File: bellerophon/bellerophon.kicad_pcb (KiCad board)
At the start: 4 copper layers, 35 x 90 mm, 45 parts, among them Q1 ST3413A, Q2 IRLL014NPBF, Q3 IRLL014NPBF, U1 HT7350-A, U2 BNO055, U3 MPL3115A2, U4 Teensy4.0, U5 XTSD, Y1 32.768kHz

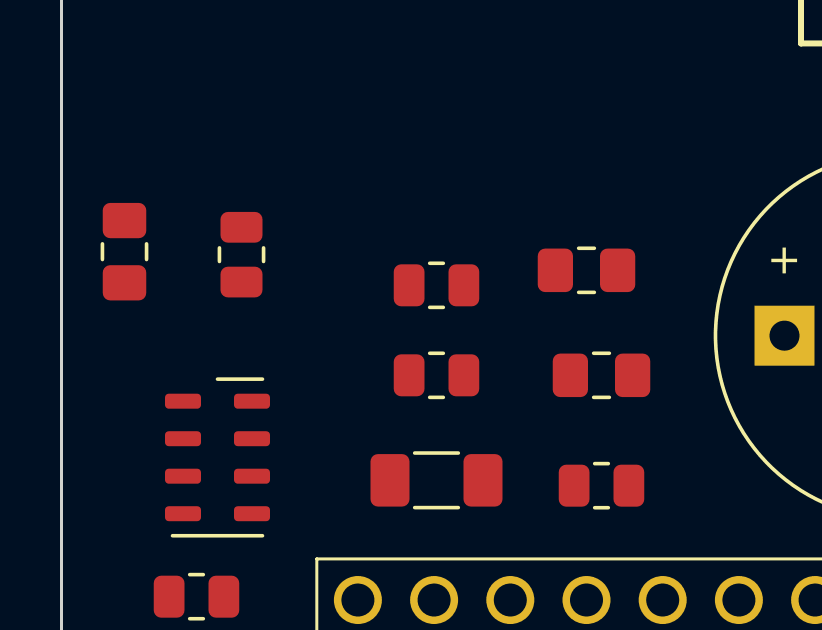
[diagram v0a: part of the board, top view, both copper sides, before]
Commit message: change pin assignments to better fit layout
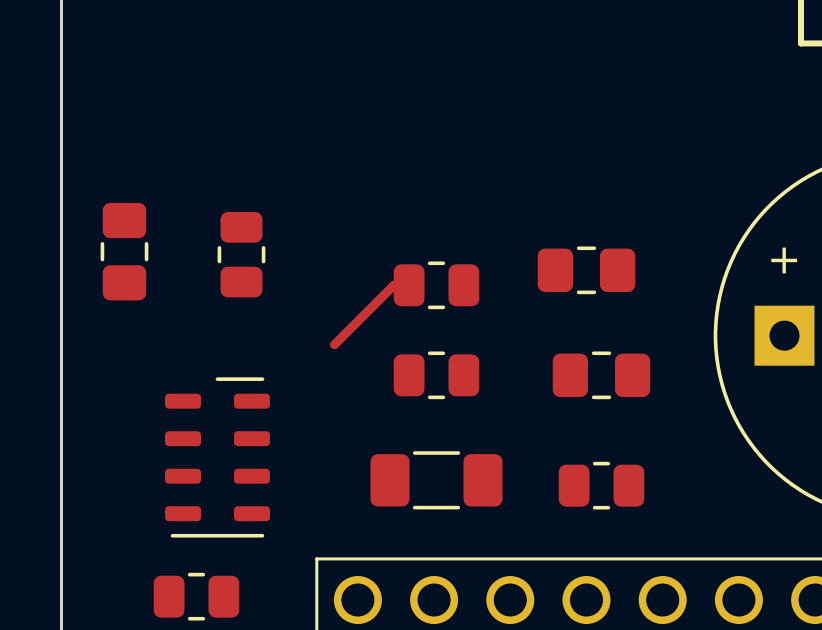
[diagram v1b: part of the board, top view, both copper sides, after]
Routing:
- net /SDA0: track 0.00 -> 3.31 mm
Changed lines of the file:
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@@
   )
   (segment (start 207.65 115.7) (end 207.65 116.3) (width 0.3) (layer "F.Cu") (net 1))
+  (segment (start 213.57868 103.62132) (end 211.6 105.6) (width 0.3) (layer "F.Cu") (net 12))
+  (segment (start 214.0875 103.62132) (end 213.57868 103.62132) (width 0.3) (layer "F.Cu") (net 12))
 )

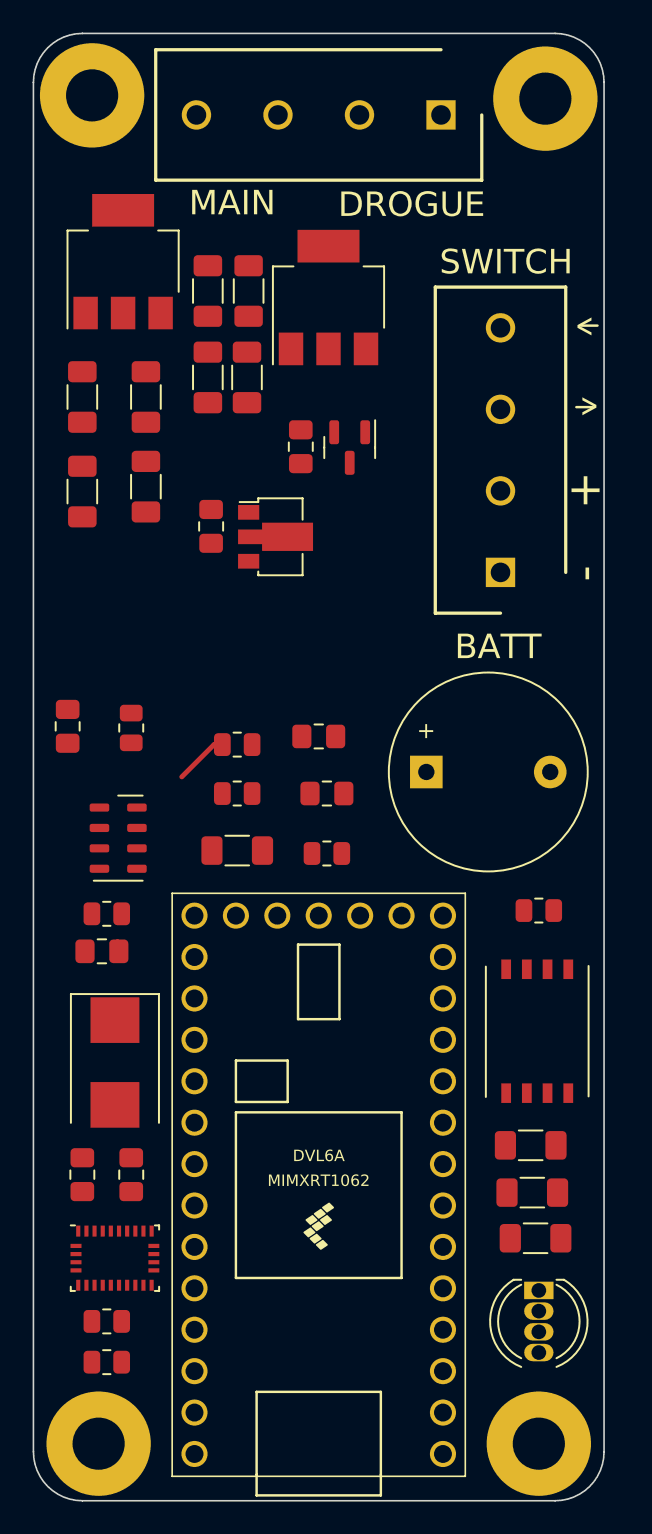
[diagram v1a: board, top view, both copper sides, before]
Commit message: change pyro mosfet to smaller SOT-23, shrink board to 85 mm
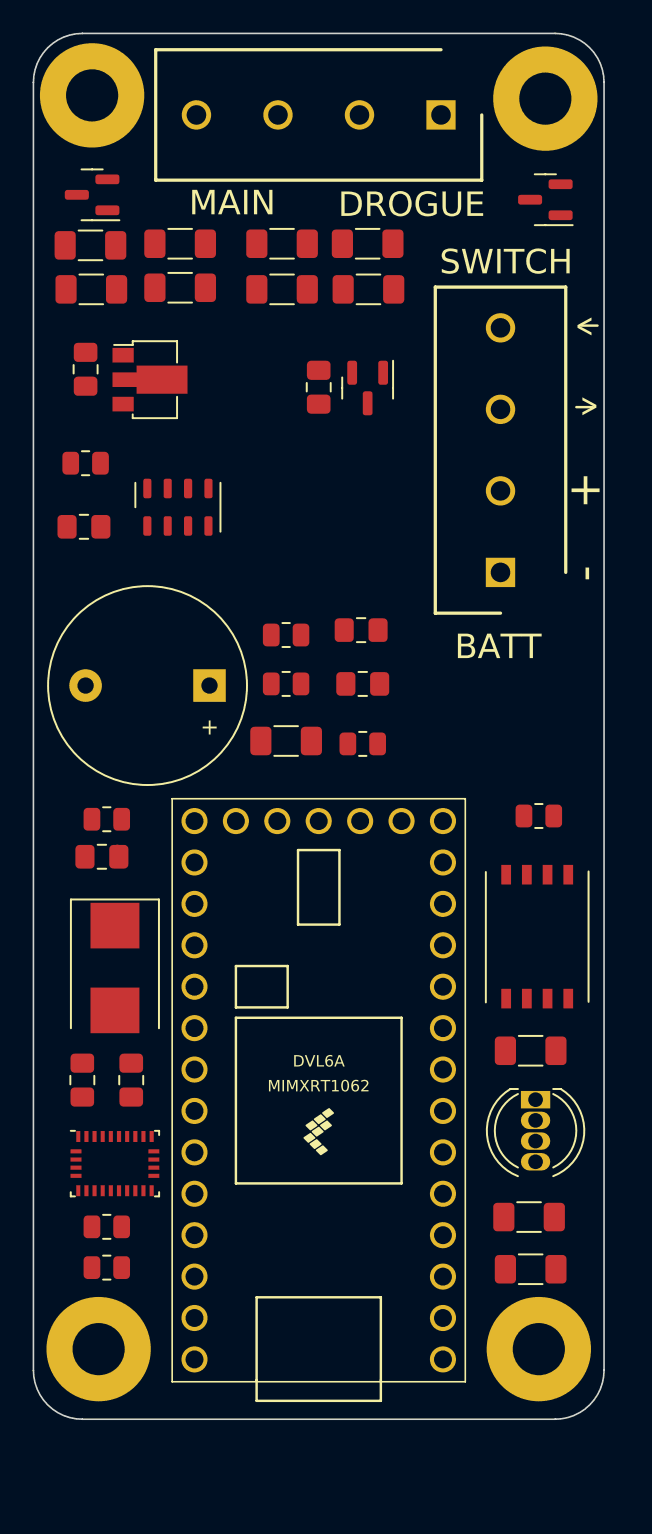
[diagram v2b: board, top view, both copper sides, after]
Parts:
- Q2, Q3: value IRLL014NPBF -> SPP3414S23RG; footprint Package_TO_SOT_SMD:SOT-223-3_TabPin2 -> Package_TO_SOT_SMD:SOT-23
- moved U3 20.6 mm to (211.4, 89.1), turned to 90 degrees
- moved R6 16.5 mm to (205.7, 86.4), turned to 180 degrees
- moved R20 15.0 mm to (211.5, 72.9), turned to 0 degrees
- moved Q2 14.6 mm to (233.9, 70.2), turned to 180 degrees
- moved BZ1 14.3 mm to (213.3, 100.0), turned to 180 degrees
- moved R16 13.9 mm to (211.5, 75.6), turned to 180 degrees
- moved C2 12.3 mm to (205.7, 80.6)
- moved U1 12.3 mm to (209.7, 81.2)
- moved C6 12.3 mm to (205.6, 90.3), turned to 180 degrees
- moved D1 11.7 mm to (233.3, 125.4)
- moved R19 9.90 mm to (206.0, 73.0), turned to 0 degrees
- moved R14 9.85 mm to (223.1, 75.7), turned to 0 degrees
- moved R13 8.48 mm to (217.8, 72.9), turned to 0 degrees
- moved R15 7.85 mm to (223.0, 72.9), turned to 0 degrees
- moved R11 7.36 mm to (218.0, 103.4)
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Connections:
- U4 pad 10: RGB3 -> PY2_TEST
- U4 pad 11: unconnected-(U4-Pad11) -> PY2
- U4 pad 21: RGB1 -> unconnected-(U4-Pad21)
- U4 pad 22: RGB2 -> unconnected-(U4-Pad22)
- U4 pad 3: unconnected-(U4-Pad3) -> RGB2
- U4 pad 4: PY1_TEST -> RGB1
- U4 pad 5: PY1 -> unconnected-(U4-Pad5)
- U4 pad 6: PY2_TEST -> RGB3
- U4 pad 7: PY2 -> BZR1
- U4 pad 8: unconnected-(U4-Pad8) -> PY1_TEST
- U4 pad 9: BZR1 -> PY1
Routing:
- net /SDA0: track 3.31 -> 0.00 mm
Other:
- board size 35 x 90 mm -> 35 x 85 mm

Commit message: change BNO055 crystal to 3215 SMD
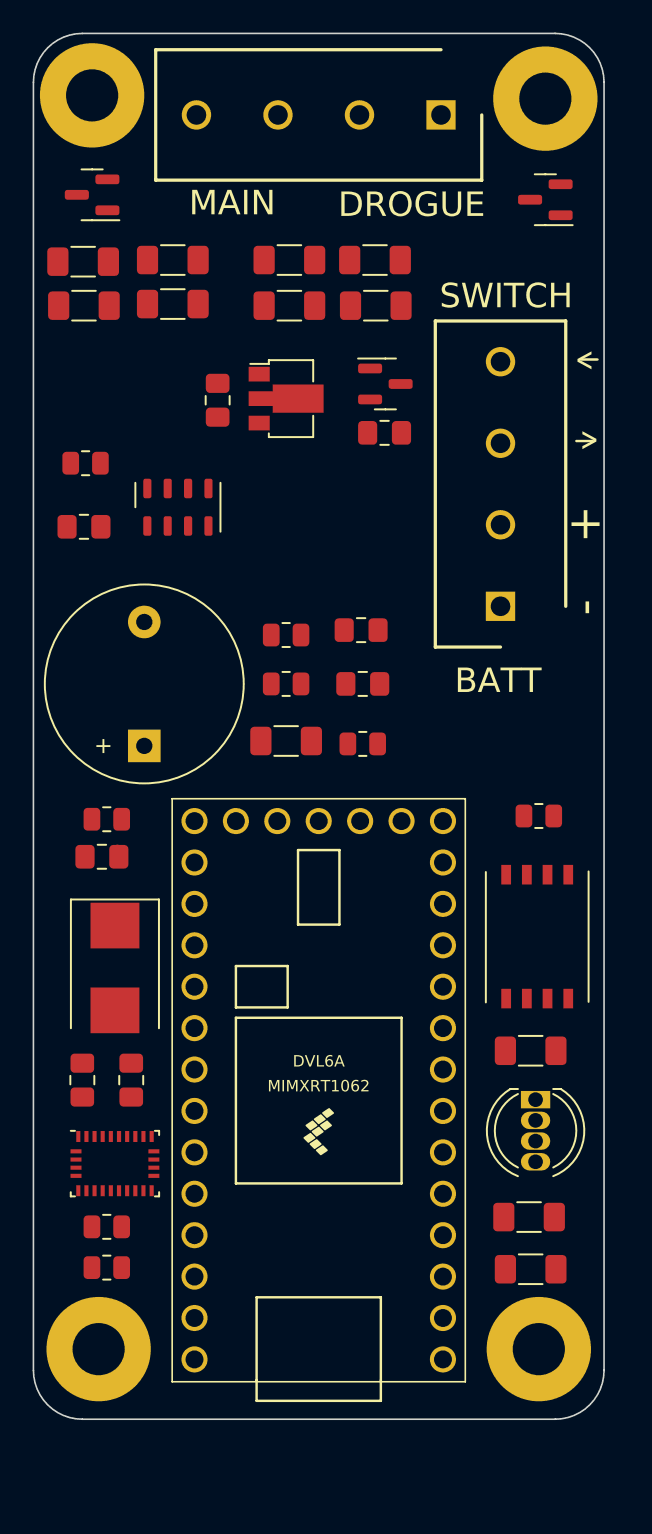
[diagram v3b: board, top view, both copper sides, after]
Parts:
- moved U1 8.43 mm to (218.0, 82.4)
- moved C2 8.32 mm to (213.8, 82.5)
- moved BZ1 5.45 mm to (209.3, 103.7), turned to 90 degrees
- moved C1 4.91 mm to (224.0, 84.5), turned to 180 degrees
- moved TERMINAL1 2.08 mm to (231.2, 95.1)
- moved Q1 1.12 mm to (224.1, 81.5), turned to 0 degrees
- moved R18 1.10 mm to (205.6, 76.7)
- moved R12 1.10 mm to (218.2, 76.7)
- moved R13 1.10 mm to (218.2, 73.9)
- moved R14 1.10 mm to (223.5, 76.7)
- moved R15 1.10 mm to (223.4, 73.9)
- moved R16 1.10 mm to (211.1, 76.6)
- moved R19 1.10 mm to (205.6, 74.0)
- moved R20 1.10 mm to (211.1, 73.9)
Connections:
- U4 pad 21: unconnected-(U4-Pad21) -> BZR1
- U4 pad 7: BZR1 -> unconnected-(U4-Pad7)

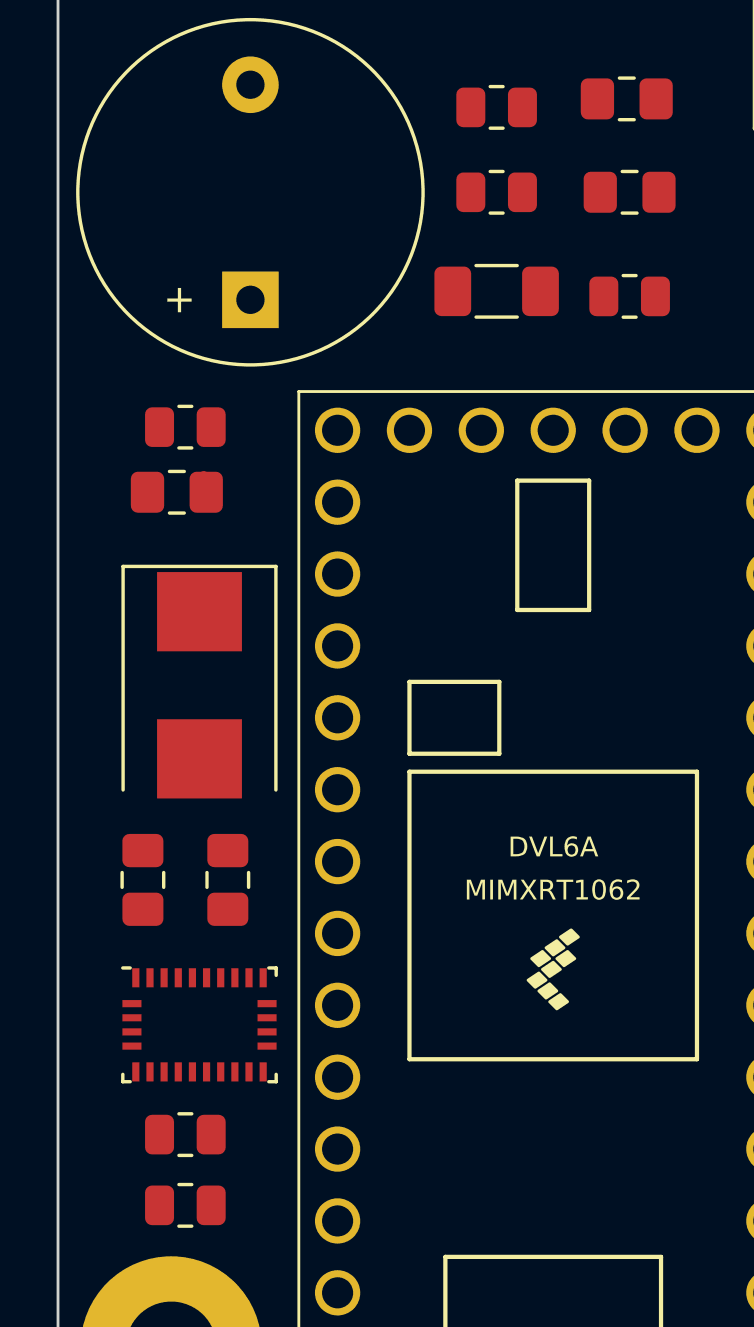
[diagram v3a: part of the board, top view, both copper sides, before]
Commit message: remove interupt, reboot and I2Caddress connection from BNO055
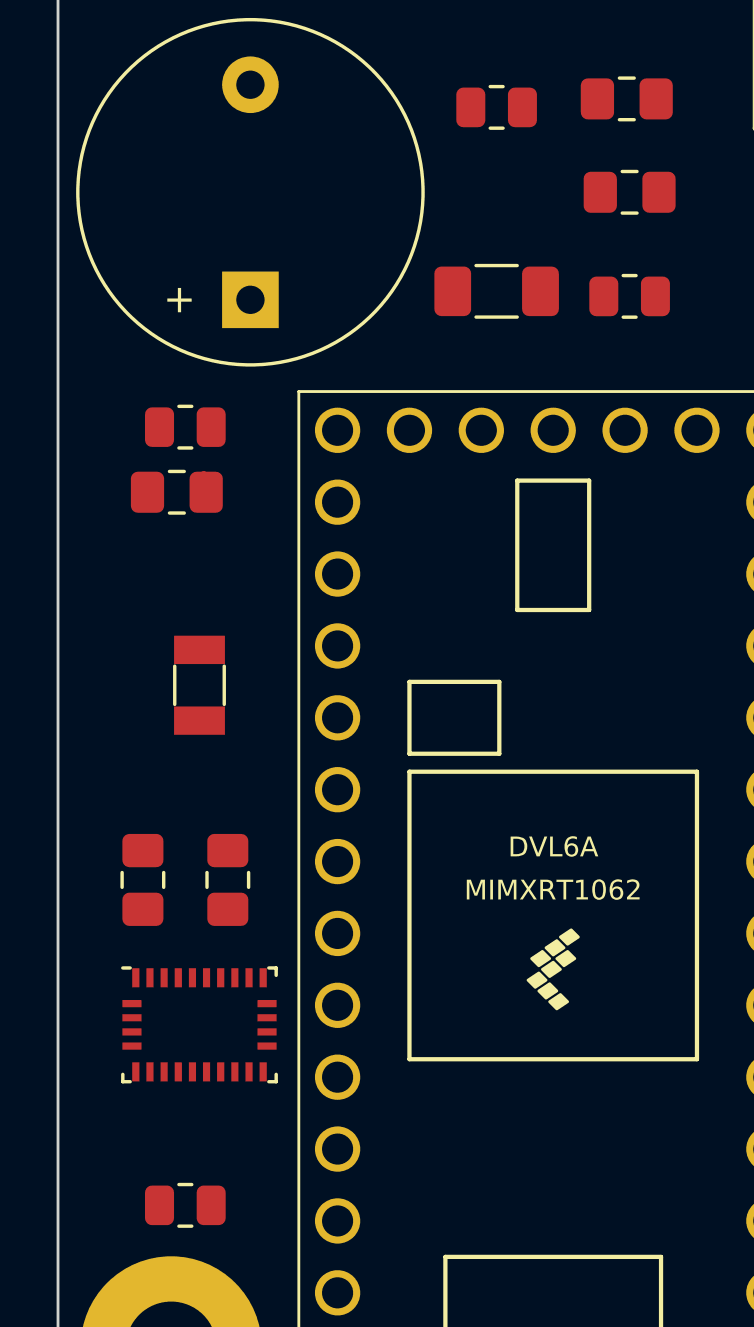
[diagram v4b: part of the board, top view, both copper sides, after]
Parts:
- removed R10, R9: 10k, Resistor_SMD:R_0805_2012Metric
- Y1: footprint Crystal:Crystal_SMD_7050-2Pin_7.0x5.0mm -> Crystal:Crystal_SMD_3215-2Pin_3.2x1.5mm
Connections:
- U2 pad 11: /NRESET_3V -> unconnected-(U2-Pad11)
- U2 pad 14: /INT_3V -> unconnected-(U2-Pad14)
- U2 pad 17: /I2CADDR_3V -> unconnected-(U2-Pad17)

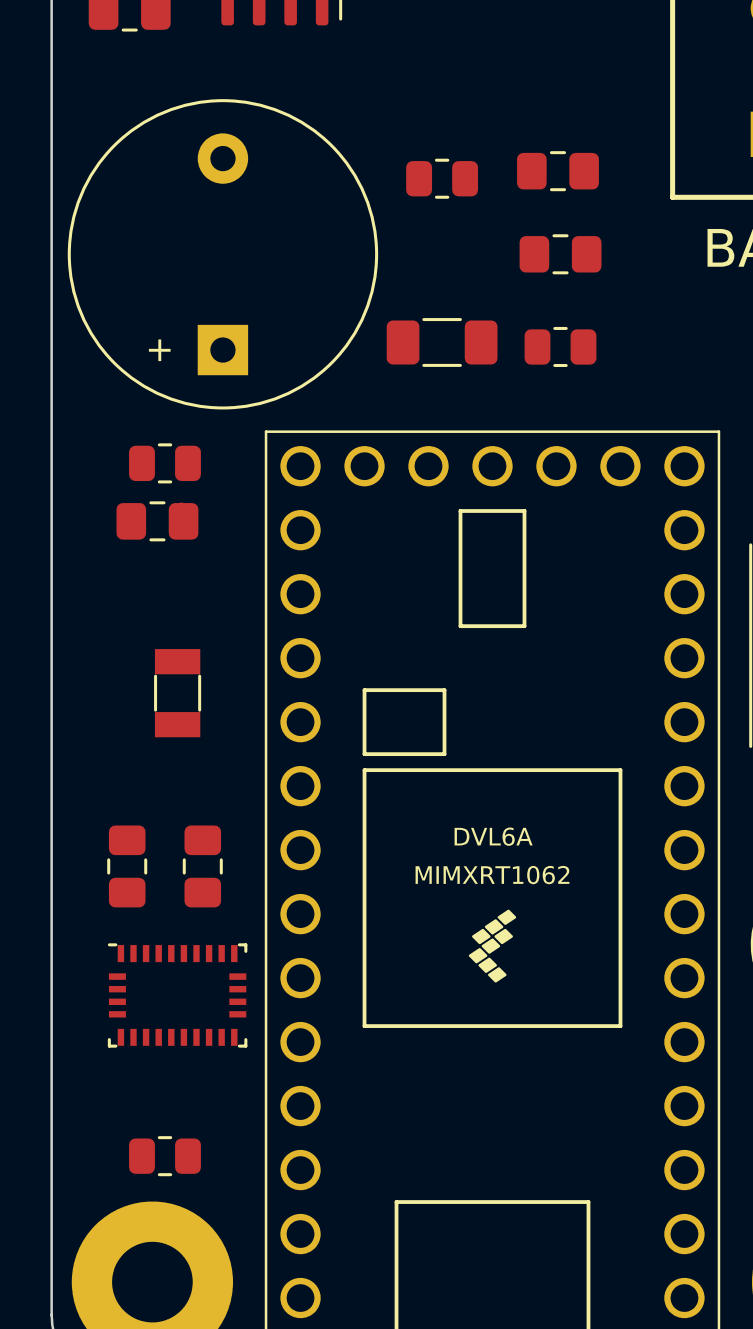
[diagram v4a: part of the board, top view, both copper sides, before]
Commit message: finalized bno055 circuitry and placement
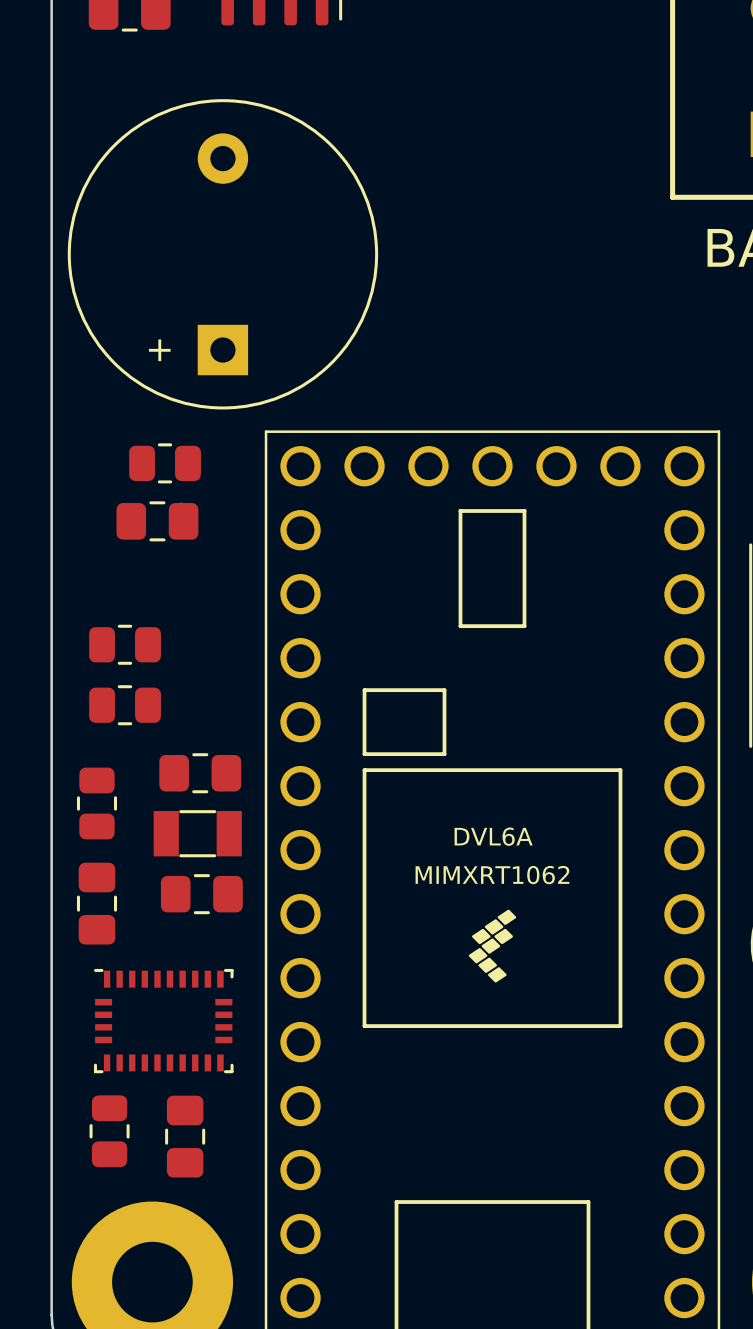
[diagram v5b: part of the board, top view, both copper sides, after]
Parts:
- R11: footprint Resistor_SMD:R_1206_3216Metric_Pad1.30x1.75mm_HandSolder -> Resistor_SMD:R_0805_2012Metric
- moved C5 41.1 mm to (207.8, 134.9), turned to -90 degrees
- moved R4 25.8 mm to (204.3, 121.7), turned to 90 degrees
- moved C4 25.1 mm to (208.4, 120.5), turned to 180 degrees
- moved R8 22.4 mm to (205.4, 115.4), turned to 180 degrees
- moved R11 19.1 mm to (205.4, 117.8), turned to 180 degrees
- moved Y1 5.64 mm to (208.3, 122.9), turned to 0 degrees
- moved R5 2.41 mm to (204.8, 134.7), turned to -90 degrees
- moved C7 1.90 mm to (204.3, 125.7), turned to 90 degrees
- moved U2 1.16 mm to (206.9, 130.3)
- moved C3 1.10 mm to (208.5, 125.3), turned to 0 degrees
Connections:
- net Net-(C3-Pad1) renamed /XIN32
- net Net-(C4-Pad1) renamed /XOUT32
- net Net-(C5-Pad1) renamed /CAP
- net Net-(C7-Pad1) renamed /VDD
- net Net-(R5-Pad1) renamed /PS0_3V
